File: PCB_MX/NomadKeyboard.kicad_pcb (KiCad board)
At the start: 2 copper layers, 159.9 x 129.6 mm, 98 parts, among them J1 4PIN, J2 OLED, SW1 SW_PUSH_LED, SW10 SW_PUSH_LED, SW11 SW_PUSH_LED, SW12 SW_PUSH_LED, SW13 SW_PUSH_LED, SW14 SW_PUSH_LED, SW15 SW_PUSH_LED, SW16 SW_PUSH_LED, SW17 SW_PUSH_LED, SW18 SW_PUSH_LED, SW19 SW_PUSH_LED, SW2 SW_PUSH_LED, SW20 SW_PUSH_LED, SW21 SW_PUSH_LED, SW22 SW_PUSH_LED, SW23 SW_PUSH_LED, SW24 SW_PUSH_LED, SW25 SW_PUSH_LED, SW26 SW_PUSH_LED, SW27 SW_PUSH_LED, SW28 SW_PUSH_LED, SW29 SW_PUSH_LED, SW3 SW_PUSH_LED, SW30 SW_PUSH_LED, SW31 SW_PUSH_LED, SW32 SW_PUSH_LED, SW33 SW_PUSH_LED, SW34 SW_PUSH_LED, SW4 SW_PUSH_LED, SW5 SW_PUSH_LED, SW6 SW_PUSH_LED, SW7 SW_PUSH_LED, SW8 SW_PUSH_LED, SW9 SW_PUSH_LED

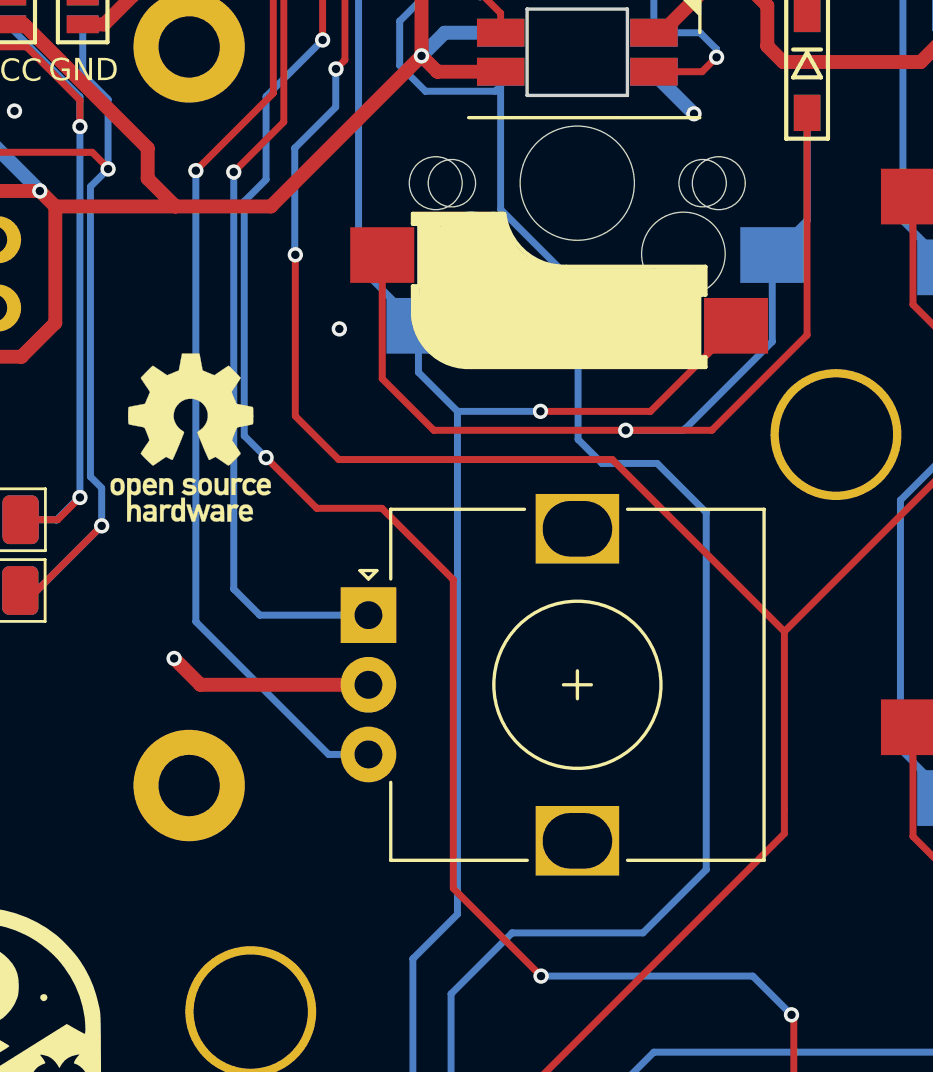
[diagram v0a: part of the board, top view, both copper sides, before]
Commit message: Tweaked position of rotary encoder, updated Gerber files
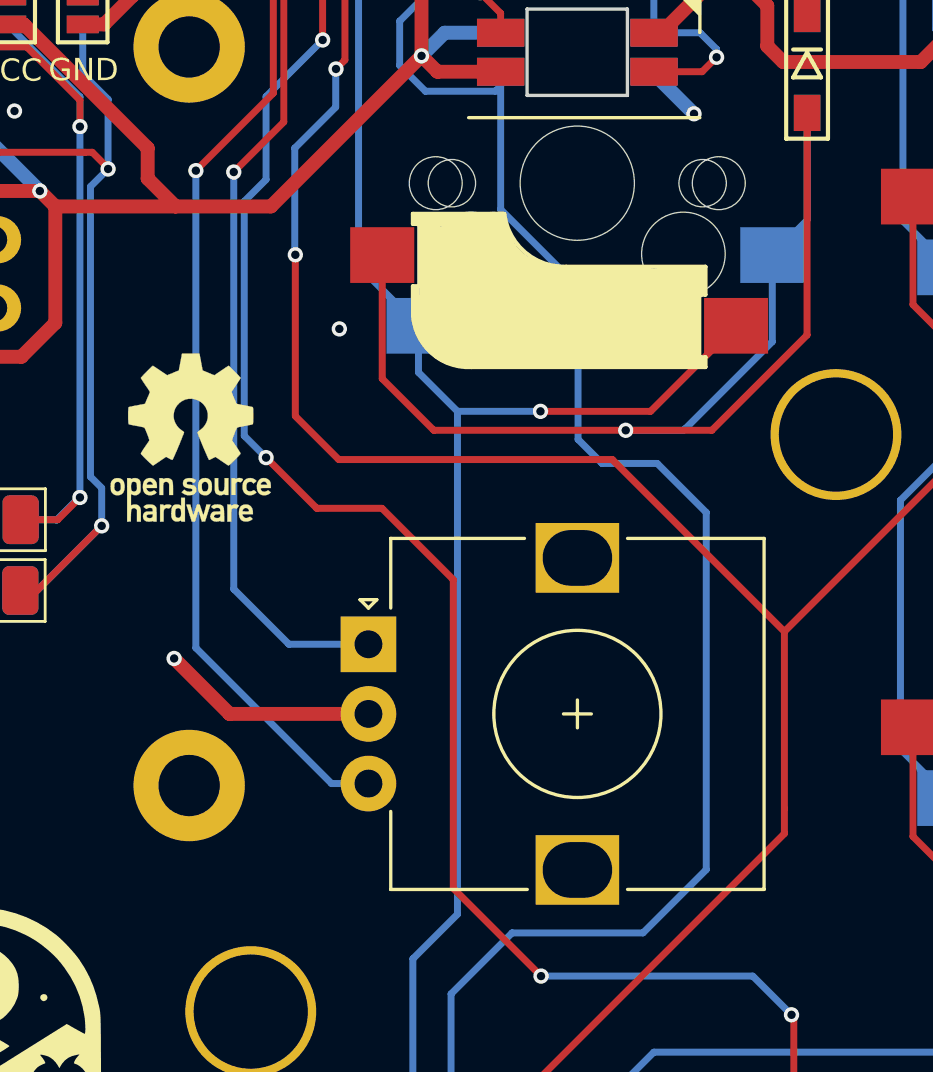
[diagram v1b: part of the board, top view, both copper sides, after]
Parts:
- moved RE1 1.05 mm to (94.0, 106.8)
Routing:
- net ENCB: track 51.2 -> 52.2 mm
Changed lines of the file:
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@@
 		(fp_arc
 			(start -2.616318 -1.12147)
-			(mid -1.868709 -2.486118)
+			(mid -1.868709 -2.486117)
 			(end -0.4 -3)
 			(stroke
@@
 	(footprint "Rotary_Encoder:RotaryEncoder_Alps_EC12E_Vertical_H20mm"
 		(layer "F.Cu")
-		(at 93.99412 105.70764)
+		(at 93.99412 106.75264)
 		(descr "Alps rotary encoder, EC12E..., vertical shaft, http://www.alps.com/prod/info/E/HTML/Encoder/Incremental/EC12E/EC12E1240405.html")
 		(tags "rotary encoder")
@@
 		(fp_arc
 			(start -2.616318 -1.12147)
-			(mid -1.868709 -2.486118)
+			(mid -1.868709 -2.486117)
 			(end -0.4 -3)
 			(stroke
@@
 	)
 	(gr_line
-		(start 73.481106 137.59264)
-		(end 86.481106 160.1093)
-		(stroke
-			(width 0.15)
-			(type default)
-		)
-		(layer "Dwgs.User")
-	)
-	(gr_line
-		(start 111.0141 116.6766)
-		(end 91.96912 116.6766)
+		(start 111.0141 118.79264)
+		(end 91.964099 118.79264)
 		(stroke
 			(width 0.15)
@@
 	(gr_line
 		(start 79.93612 43.65264)
-		(end 79.93612 133.80264)
+		(end 79.93612 137.85264)
 		(stroke
 			(width 0.15)
@@
 	)
 	(gr_line
-		(start 91.9641 99.7276)
-		(end 91.96912 116.6766)
-		(stroke
-			(width 0.15)
-			(type default)
-		)
-		(layer "Dwgs.User")
-	)
-	(gr_line
-		(start 73.481106 137.59264)
-		(end 106.476674 118.54264)
-		(stroke
-			(width 0.15)
-			(type default)
-		)
-		(layer "Dwgs.User")
-	)
-	(gr_line
-		(start 106.476674 118.54264)
-		(end 119.476674 141.0593)
+		(start 111.0141 116.6766)
+		(end 111.0141 118.79264)
 		(stroke
 			(width 0.15)
@@
 	)
 	(gr_line
-		(start 86.481106 160.1093)
-		(end 119.476674 141.0593)
+		(start 91.9641 99.73264)
+		(end 91.9641 118.787681)
 		(stroke
 			(width 0.15)
@@
 	)
 	(segment
-		(start 93.99412 108.20764)
-		(end 87.96412 108.20764)
-		(width 0.5)
-		(layer "F.Cu")
-		(net 29)
-	)
-	(segment
 		(start 84.02912 48.3994)
 		(end 84.52588 47.90264)
@@
 	)
 	(segment
-		(start 87.96412 108.20764)
-		(end 87.01912 107.26264)
-		(width 0.5)
-		(layer "F.Cu")
-		(net 29)
-	)
-	(segment
 		(start 161.3991 77.7026)
 		(end 161.72916 77.7026)
@@
 	)
 	(segment
+		(start 93.99412 109.25264)
+		(end 89.00912 109.25264)
+		(width 0.5)
+		(layer "F.Cu")
+		(net 29)
+	)
+	(segment
 		(start 199.4991 63.00266)
 		(end 200.08912 62.41264)
@@
 	)
 	(segment
+		(start 89.00912 109.25264)
+		(end 87.01912 107.26264)
+		(width 0.5)
+		(layer "F.Cu")
+		(net 29)
+	)
+	(segment
 		(start 142.3391 80.2026)
 		(end 142.69916 80.2026)
@@
 	)
 	(segment
-		(start 89.15912 89.80264)
-		(end 89.15912 104.77264)
+		(start 77.55812 78.25764)
+		(end 87.08412 78.25764)
 		(width 0.25)
 		(layer "B.Cu")
@@
 	)
 	(segment
-		(start 77.55812 78.25764)
-		(end 87.08412 78.25764)
+		(start 74.86988 75.5694)
+		(end 77.55812 78.25764)
 		(width 0.25)
 		(layer "B.Cu")
@@
 	)
 	(segment
-		(start 74.86988 75.5694)
-		(end 77.55812 78.25764)
+		(start 93.99412 106.75264)
+		(end 91.13912 106.75264)
 		(width 0.25)
 		(layer "B.Cu")
@@
 	)
 	(segment
-		(start 90.09412 105.70764)
-		(end 93.99412 105.70764)
+		(start 91.13912 106.75264)
+		(end 89.15912 104.77264)
 		(width 0.25)
 		(layer "B.Cu")
@@
 	(segment
 		(start 89.15912 104.77264)
-		(end 90.09412 105.70764)
+		(end 89.15912 89.80264)
 		(width 0.25)
 		(layer "B.Cu")
@@
 	)
 	(segment
-		(start 92.56412 110.70764)
-		(end 93.99412 110.70764)
+		(start 87.79912 106.88264)
+		(end 92.66912 111.75264)
 		(width 0.25)
 		(layer "B.Cu")
@@
 	)
 	(segment
-		(start 87.79912 105.94264)
-		(end 92.56412 110.70764)
+		(start 84.60912 77.07264)
+		(end 78.91312 77.07264)
 		(width 0.25)
 		(layer "B.Cu")
@@
 	)
 	(segment
-		(start 84.60912 77.07264)
-		(end 78.91312 77.07264)
+		(start 84.60912 77.09264)
+		(end 84.60912 77.07264)
 		(width 0.25)
 		(layer "B.Cu")
@@
 	)
 	(segment
-		(start 84.60912 77.09264)
-		(end 84.60912 77.07264)
+		(start 92.66912 111.75264)
+		(end 93.99412 111.75264)
 		(width 0.25)
 		(layer "B.Cu")
@@
 	(segment
 		(start 87.79912 89.75264)
-		(end 87.79912 105.94264)
+		(end 87.79912 106.88264)
 		(width 0.25)
 		(layer "B.Cu")
